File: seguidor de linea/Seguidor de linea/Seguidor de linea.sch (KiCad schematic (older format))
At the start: 16 parts, among them IC1 MC9S08QG8xPBE, J1 PWM MOTORES DC, J2 Reprogramacion del micro, J3 Conn_01x02_Female, J4 Conn_01x02_Female, J5 Conn_01x02_Female, J6 Conn_01x02_Female, U1 CNY70, U2 CNY70

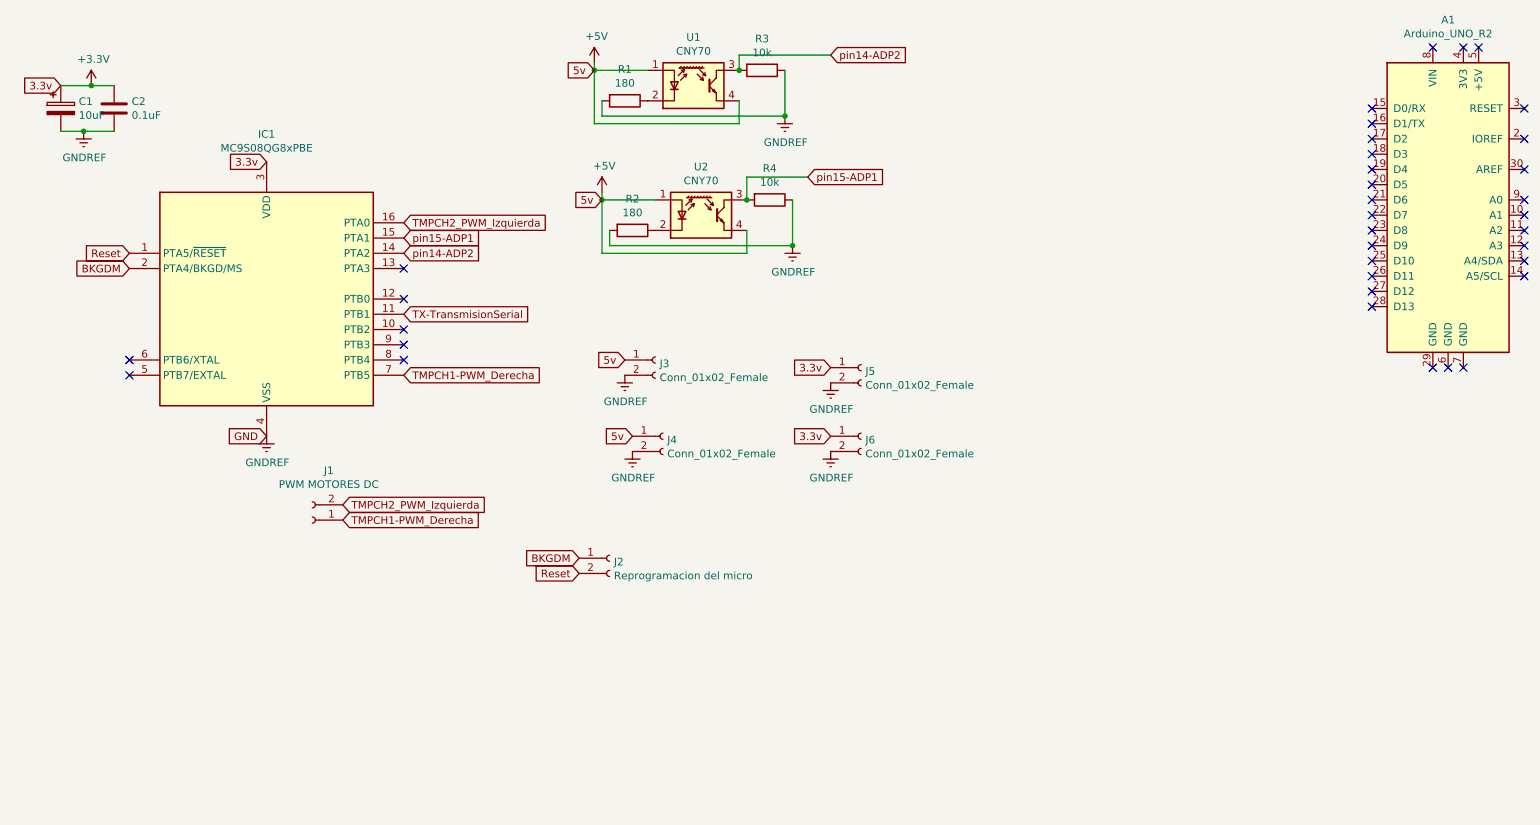
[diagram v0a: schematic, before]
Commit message: pdf y cad del seguidor de linea, con planos explosionados
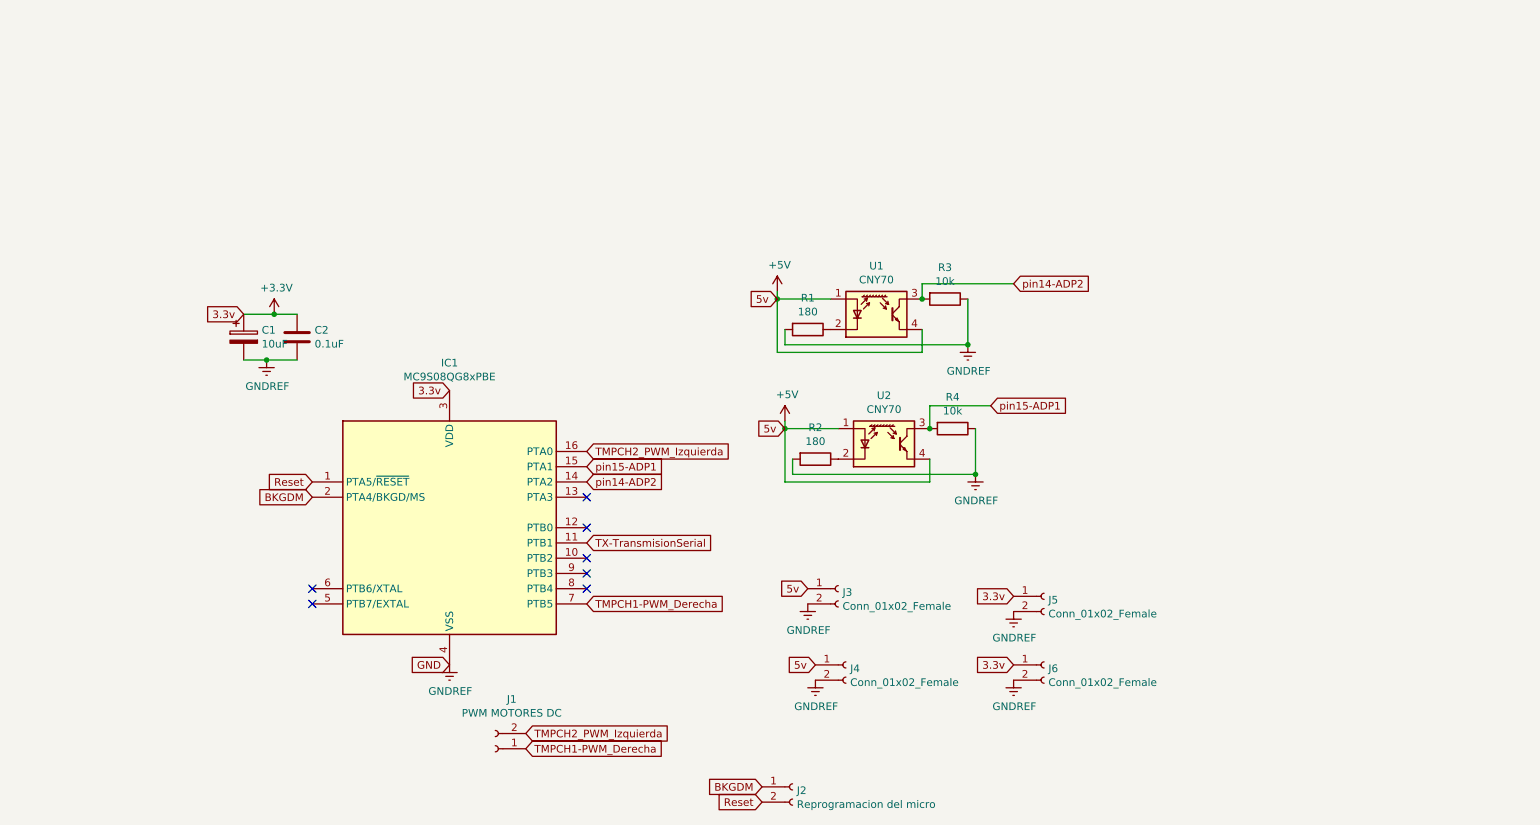
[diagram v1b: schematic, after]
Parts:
- removed A1: Arduino_UNO_R2, Module:Arduino_UNO_R2, symbol MCU_Module:Arduino_UNO_R2
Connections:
- no-connect marks 36 -> 7
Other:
- moved on the sheet: C1, C2, IC1, J1, J2, J3, J4, J5, J6, R1, R2, R3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
